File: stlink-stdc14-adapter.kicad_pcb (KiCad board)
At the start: 2 copper layers, 34.3 x 50.8 mm, 7 parts, among them J1 Conn_ST_STDC14, J2 Conn_ARM_JTAG_SWD_20, J3 Conn_01x04

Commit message: swap RX and TX on the UART header
Yep, I was wrong on the 50/50 guess, as is tradition.
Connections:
- J3 pad 2: /UART_RX -> /UART_TX
- J3 pad 3: /UART_TX -> /UART_RX
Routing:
- net GND: track 12.1 -> 3.45 mm
- net /UART_RX: track 18.2 -> 14.2 mm
- net /UART_TX: track 12.9 -> 15.5 mm
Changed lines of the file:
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@@
 			(layers "*.Cu" "*.Mask")
 			(remove_unused_layers no)
-			(net "/UART_RX")
+			(net "/UART_TX")
 			(pinfunction "Pin_2_2")
 			(pintype "passive")
@@
 			(layers "*.Cu" "*.Mask")
 			(remove_unused_layers no)
-			(net "/UART_TX")
+			(net "/UART_RX")
 			(pinfunction "Pin_3_3")
 			(pintype "passive")
@@
 			(pinfunction "GND_5")
 			(pintype "power_in")
+			(thermal_bridge_width 0.508)
+			(thermal_bridge_angle 90)
+			(thermal_gap 0.254)
 		)
 		(pad "6" thru_hole circle
@@
 			(pinfunction "GND_7")
 			(pintype "passive")
+			(thermal_bridge_width 0.508)
+			(thermal_bridge_angle 90)
+			(thermal_gap 0.254)
 		)
 		(pad "8" thru_hole circle
@@
 			(pinfunction "GNDDetect_11")
 			(pintype "passive")
+			(thermal_bridge_width 0.508)
+			(thermal_bridge_angle 90)
+			(thermal_gap 0.254)
 		)
 		(pad "12" thru_hole circle
@@
 	)
 	(segment
+		(start 74.676 78.74)
+		(end 74.59684 78.74)
+		(width 0.508)
+		(layer "F.Cu")
+		(net "GND")
+	)
+	(segment
+		(start 73.722 77.027)
+		(end 74.549 76.2)
+		(width 0.508)
+		(layer "F.Cu")
+		(net "GND")
+	)
+	(segment
+		(start 74.549 76.2)
+		(end 74.676 76.2)
+		(width 0.508)
+		(layer "F.Cu")
+		(net "GND")
+	)
+	(segment
+		(start 73.722 77.86516)
+		(end 73.722 77.027)
+		(width 0.508)
+		(layer "F.Cu")
+		(net "GND")
+	)
+	(segment
+		(start 74.59684 78.74)
+		(end 73.722 77.86516)
+		(width 0.508)
+		(layer "F.Cu")
+		(net "GND")
+	)
+	(segment
 		(start 97.409 87.63)
 		(end 95.651 89.388)
@@
 	)
 	(segment
+		(start 78.932 80.837)
+		(end 75.503 80.837)
+		(width 0.254)
+		(layer "F.Cu")
+		(net "/UART_RX")
+	)
+	(segment
+		(start 85.725 87.63)
+		(end 78.932 80.837)
+		(width 0.254)
+		(layer "F.Cu")
+		(net "/UART_RX")
+	)
+	(segment
+		(start 75.503 80.837)
+		(end 74.676 80.01)
+		(width 0.254)
+		(layer "F.Cu")
+		(net "/UART_RX")
+	)
+	(segment
+		(start 80.645 80.01)
+		(end 75.946 80.01)
+		(width 0.254)
+		(layer "F.Cu")
+		(net "/UART_TX")
+	)
+	(segment
+		(start 88.265 87.63)
+		(end 80.645 80.01)
+		(width 0.254)
+		(layer "F.Cu")
+		(net "/UART_TX")
+	)
+	(segment
 		(start 100.43653 71.213)
 		(end 78.393 71.213)
@@
 	)
 	(segment
-		(start 74.676 74.93)
-		(end 73.722 75.884)
-		(width 0.508)
-		(layer "F.Cu")
-		(net "GND")
-	)
-	(segment
-		(start 73.722 76.446894)
-		(end 73.722 78.493106)
-		(width 0.508)
-		(layer "F.Cu")
-		(net "GND")
-	)
-	(segment
-		(start 73.722 78.493106)
-		(end 73.968894 78.74)
-		(width 0.508)
-		(layer "F.Cu")
-		(net "GND")
-	)
-	(segment
-		(start 73.968894 78.74)
-		(end 74.676 78.74)
-		(width 0.508)
-		(layer "F.Cu")
-		(net "GND")
-	)
-	(segment
-		(start 73.722 75.884)
-		(end 73.722 76.446894)
-		(width 0.508)
-		(layer "F.Cu")
-		(net "GND")
-	)
-	(segment
-		(start 73.968894 76.2)
-		(end 73.722 76.446894)
-		(width 0.508)
-		(layer "F.Cu")
-		(net "GND")
-	)
-	(segment
-		(start 74.676 76.2)
-		(end 73.968894 76.2)
-		(width 0.508)
-		(layer "F.Cu")
-		(net "GND")
-	)
-	(segment
-		(start 73.722 78.493106)
-		(end 73.968894 78.74)
-		(width 0.508)
-		(layer "B.Cu")
-		(net "GND")
-	)
-	(segment
-		(start 74.676 74.93)
-		(end 73.722 75.884)
-		(width 0.508)
-		(layer "B.Cu")
-		(net "GND")
-	)
-	(segment
-		(start 74.676 76.2)
-		(end 73.968894 76.2)
-		(width 0.508)
-		(layer "B.Cu")
-		(net "GND")
-	)
-	(segment
-		(start 73.722 75.884)
-		(end 73.722 76.446894)
-		(width 0.508)
-		(layer "B.Cu")
-		(net "GND")
-	)
-	(segment
-		(start 73.722 76.446894)
-		(end 73.722 78.493106)
-		(width 0.508)
-		(layer "B.Cu")
-		(net "GND")
-	)
-	(segment
-		(start 73.968894 76.2)
-		(end 73.722 76.446894)
-		(width 0.508)
-		(layer "B.Cu")
-		(net "GND")
-	)
-	(segment
-		(start 73.968894 78.74)
-		(end 74.676 78.74)
-		(width 0.508)
-		(layer "B.Cu")
-		(net "GND")
-	)
-	(segment
 		(start 77.123 76.107)
 		(end 98.586 76.107)
@@
 		(net "/nRESET")
 	)
-	(segment
-		(start 88.265 87.63)
-		(end 87.088 88.807)
-		(width 0.254)
-		(layer "F.Cu")
-		(net "/UART_RX")
-	)
-	(segment
-		(start 87.088 88.807)
-		(end 82.69747 88.807)
-		(width 0.254)
-		(layer "F.Cu")
-		(net "/UART_RX")
-	)
-	(segment
-		(start 74.676 80.78553)
-		(end 74.676 80.01)
-		(width 0.254)
-		(layer "F.Cu")
-		(net "/UART_RX")
-	)
-	(segment
-		(start 82.69747 88.807)
-		(end 74.676 80.78553)
-		(width 0.254)
-		(layer "F.Cu")
-		(net "/UART_RX")
-	)
-	(segment
-		(start 75.946 80.01)
-		(end 78.105 80.01)
-		(width 0.254)
-		(layer "F.Cu")
-		(net "/UART_TX")
-	)
-	(segment
-		(start 78.105 80.01)
-		(end 85.725 87.63)
-		(width 0.254)
-		(layer "F.Cu")
-		(net "/UART_TX")
-	)
 	(zone

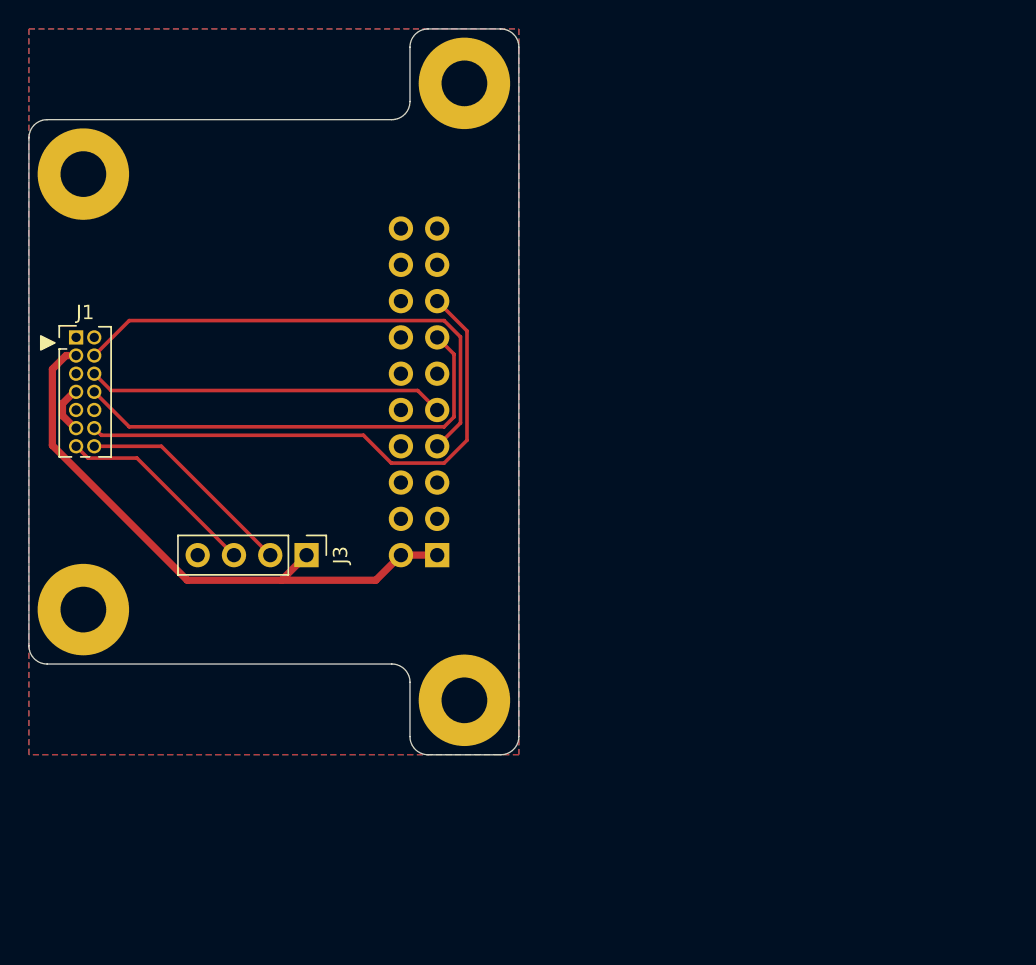
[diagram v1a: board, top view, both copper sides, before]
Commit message: kinda redo the whole layout for a smaller board
1.5" x 1" size, no more mounting holes. Smaller = cheaper.
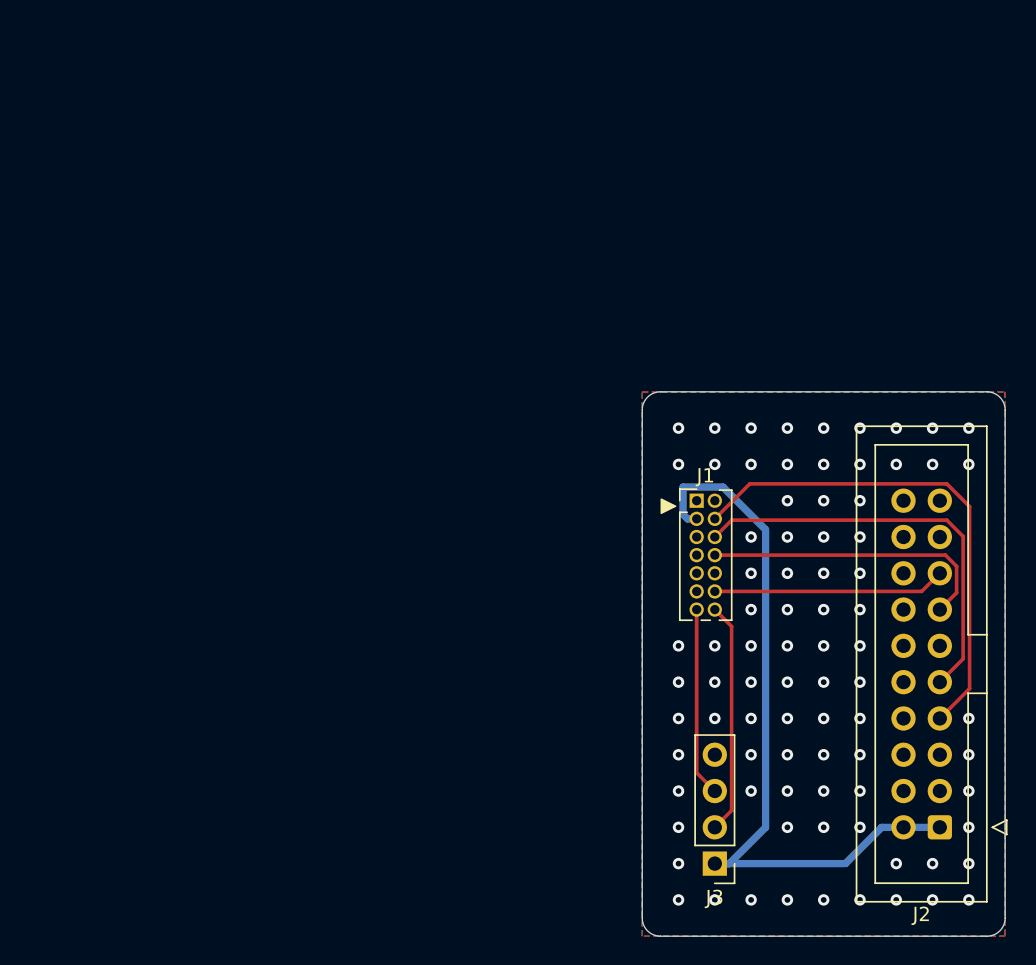
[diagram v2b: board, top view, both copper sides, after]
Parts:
- removed H1, H2, H3, H4: MountingHole_Pad, MountingHole:MountingHole_3.2mm_M3_Pad
- J2: footprint Connector_PinSocket_2.54mm:PinSocket_2x10_P2.54mm_Vertical -> Connector_IDC:IDC-Header_2x10_P2.54mm_Vertical; moved to F.Cu
- moved J1 44.9 mm to (118.1, 83.8)
- moved J2 40.0 mm to (135.1, 106.7), turned to 180 degrees
- moved J3 35.8 mm to (119.4, 109.2), turned to 180 degrees
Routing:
- net /nRESET: track 38.4 -> 16.3 mm
- net /SWO: track 32.5 -> 20.8 mm
- net VCC: track 41.4 -> 52.2 mm
- net /SWCLK: track 25.1 -> 29.2 mm
- net GND: track 3.45 -> 0.00 mm, vias 0 -> 82
- net /UART_RX: track 14.2 -> 13.2 mm
- net /UART_TX: track 15.5 -> 16.2 mm
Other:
- board size 34.3 x 50.8 mm -> 25.4 x 38.1 mm
- board text added: "{ "ViaStitching": "0.2", "stitch_zone_0": { "HSpacing": "100", "VSpacing": "100", "HOffset": "0", "VOffset": "0", "Clearance": "0", "Randomize": false } }"
- board text added: "{ "ViaStitching": "0.2", "stitch_zone_0": { "HSpacing": "100", "VSpacing": "100", "HOffset": "0", "VOffset": "0", "Clearance": "50", "Randomize": false } }"
- board text added: "{ "ViaStitching": "0.2", "stitch_zone_0": { "HSpacing": "40", "VSpacing": "40", "HOffset": "0", "VOffset": "0", "Clearance": "0", "Randomize": false } }"

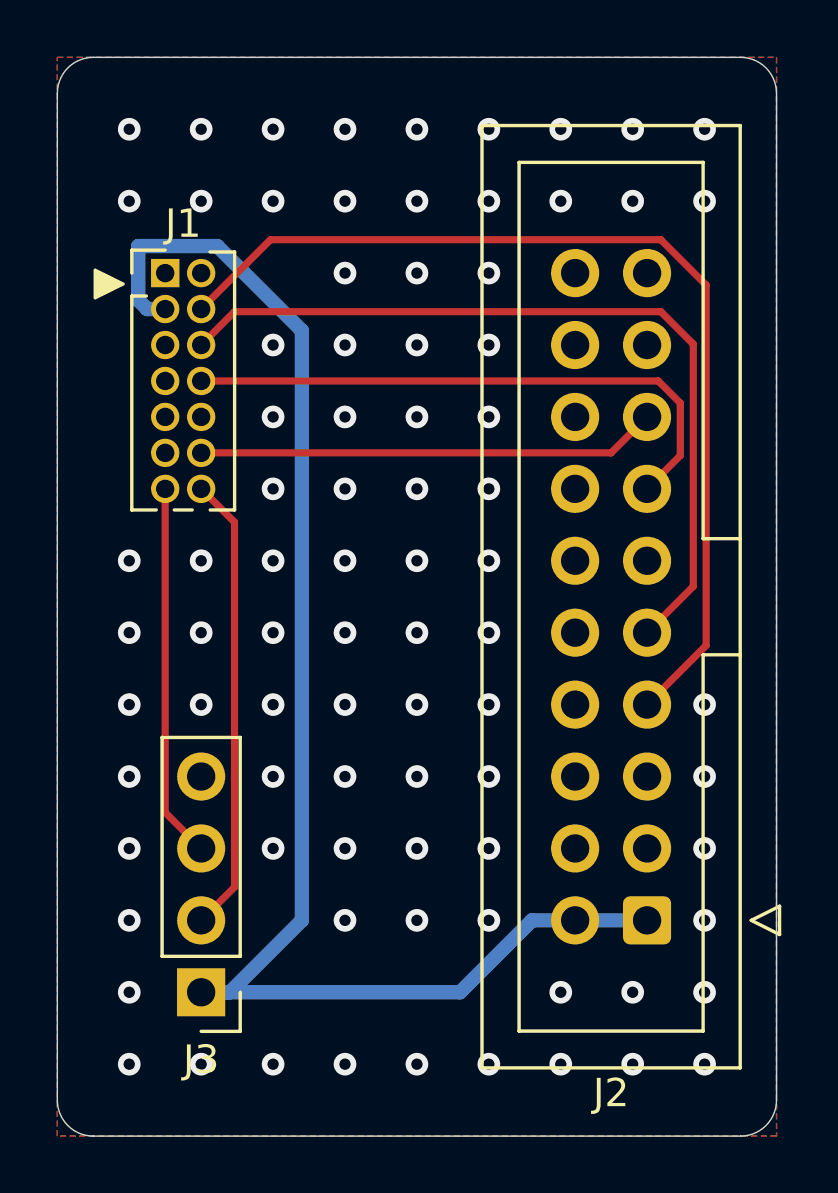
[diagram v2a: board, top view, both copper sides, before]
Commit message: re-route, add silkscreen and via stitching
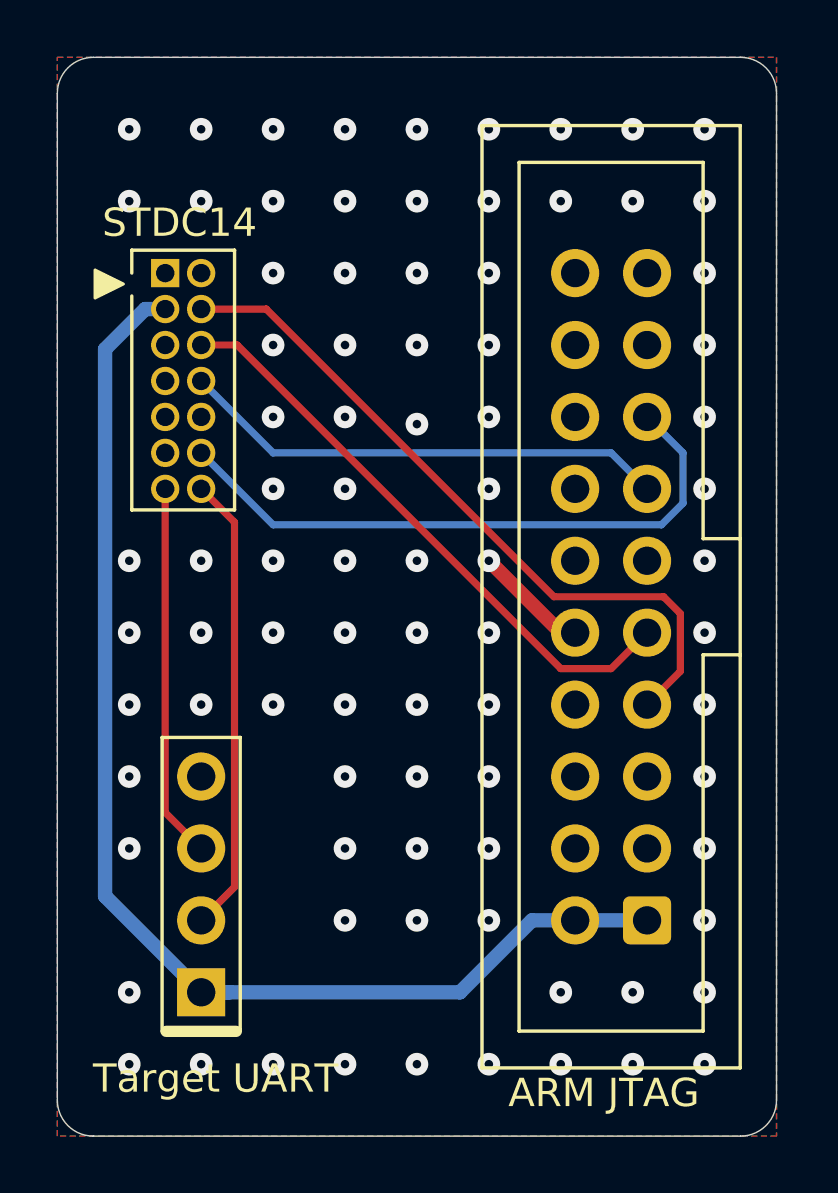
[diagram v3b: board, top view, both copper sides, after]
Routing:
- net /SWDIO: track 35.2 -> 25.1 mm
- net /SWCLK: track 29.2 -> 21.0 mm
- net VCC: track 52.2 -> 44.6 mm
- net /nRESET: track 16.3 -> 22.0 mm
- net GND: track 0.00 -> 4.10 mm, vias 82 -> 85
- net /SWO: track 20.8 -> 17.3 mm
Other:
- board text added: "STDC14 Adapter Rev A"

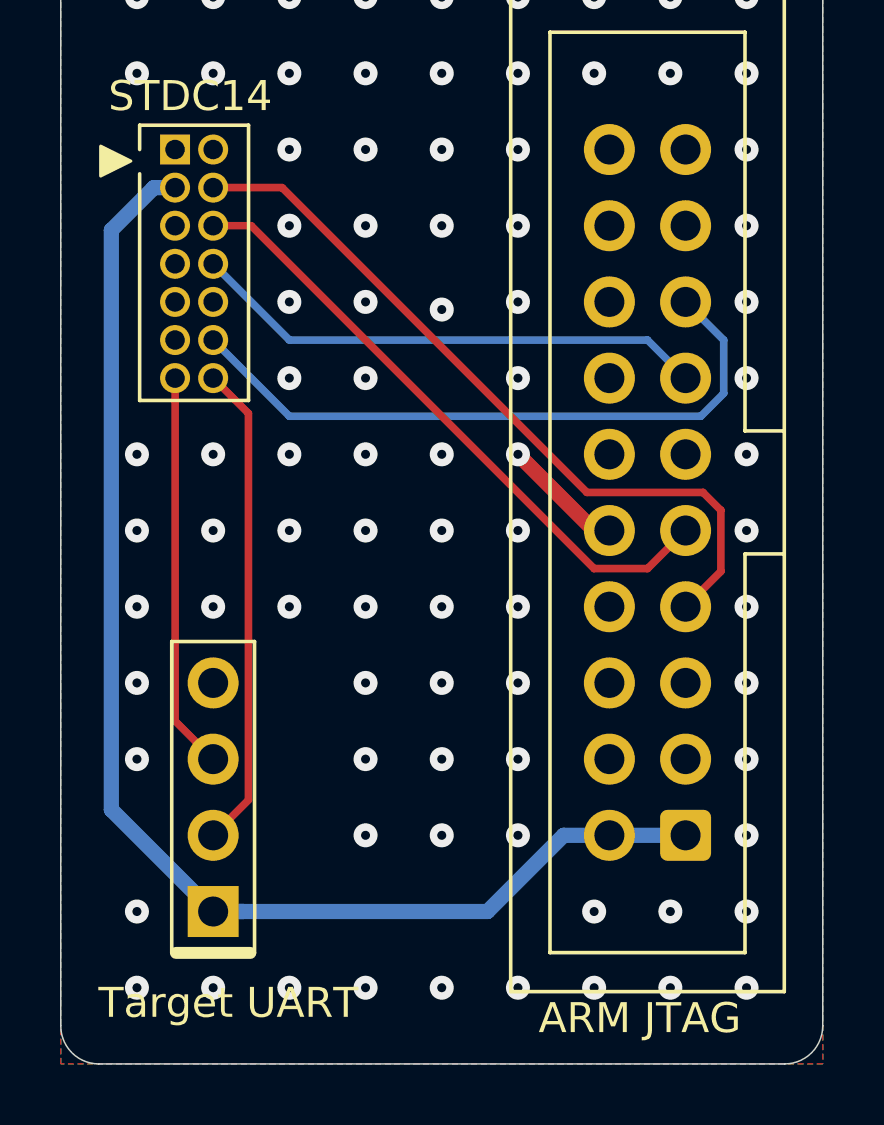
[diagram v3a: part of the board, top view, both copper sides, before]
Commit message: rotate UART header
To make more room on the side of the STDC14 so there's enough space to
grab the plug comfortably.
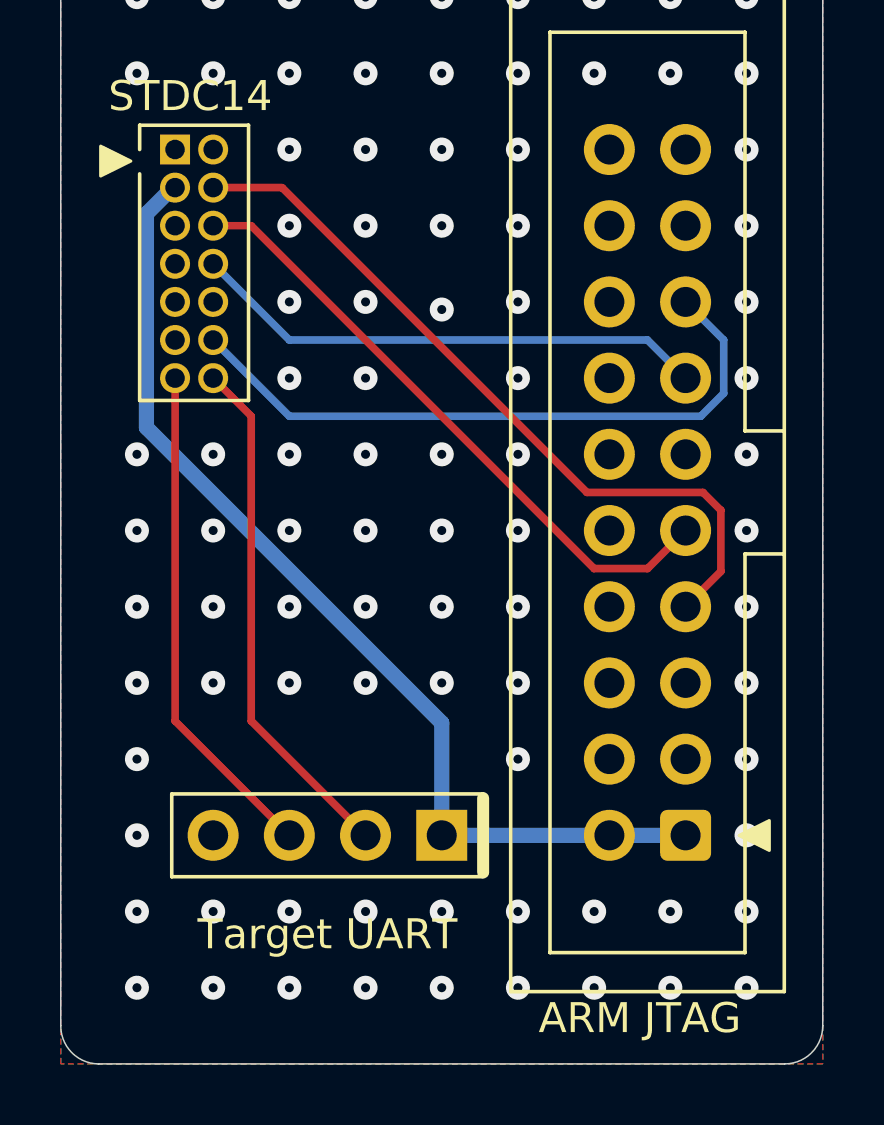
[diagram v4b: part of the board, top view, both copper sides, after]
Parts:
- moved J3 8.03 mm to (127.0, 106.7), turned to -90 degrees
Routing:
- net VCC: track 44.6 -> 34.2 mm
- net GND: track 4.10 -> 0.51 mm, vias 85 -> 88
- net /UART_RX: track 13.2 -> 16.8 mm
- net /UART_TX: track 16.2 -> 17.3 mm
